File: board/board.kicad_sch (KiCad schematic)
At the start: 22 parts, among them J1 Conn_01x10_Pin, J2 Conn_01x10, J3 Conn_01x20, J5 Conn_01x06, U1 nPM1300-CAXX

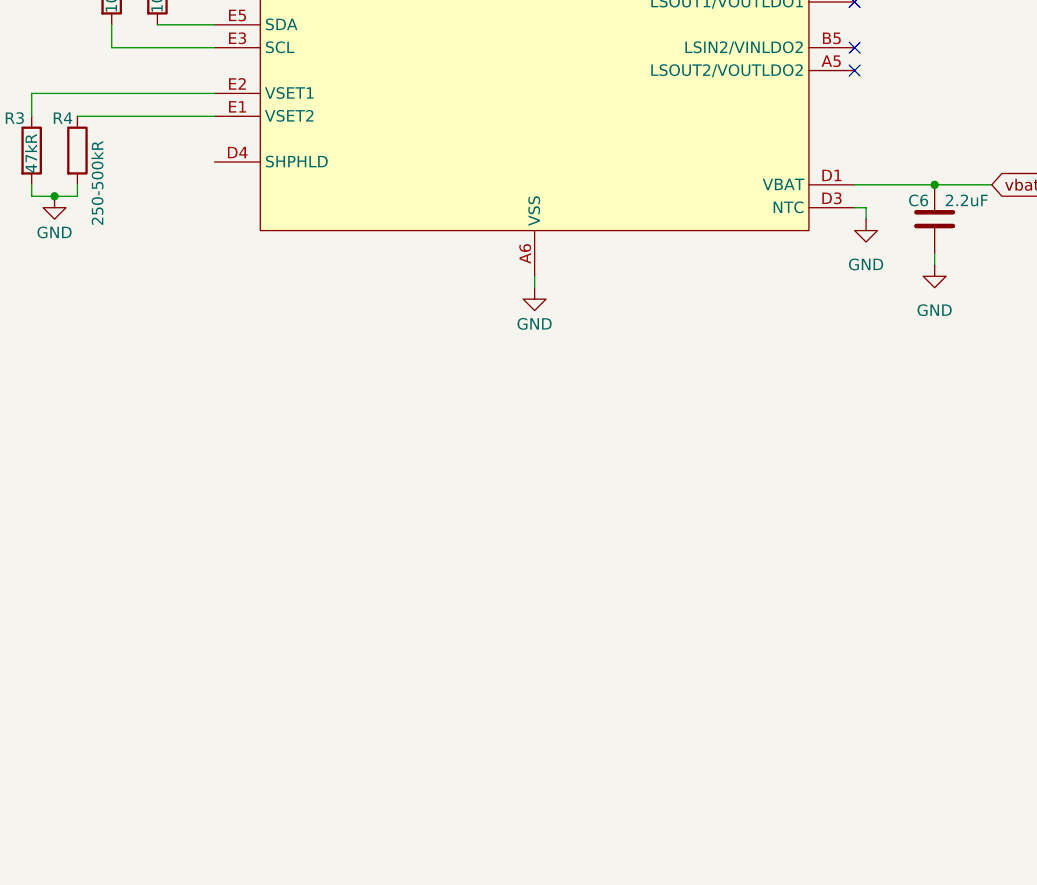
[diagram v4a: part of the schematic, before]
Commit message: board: sch tidy up and battery connector
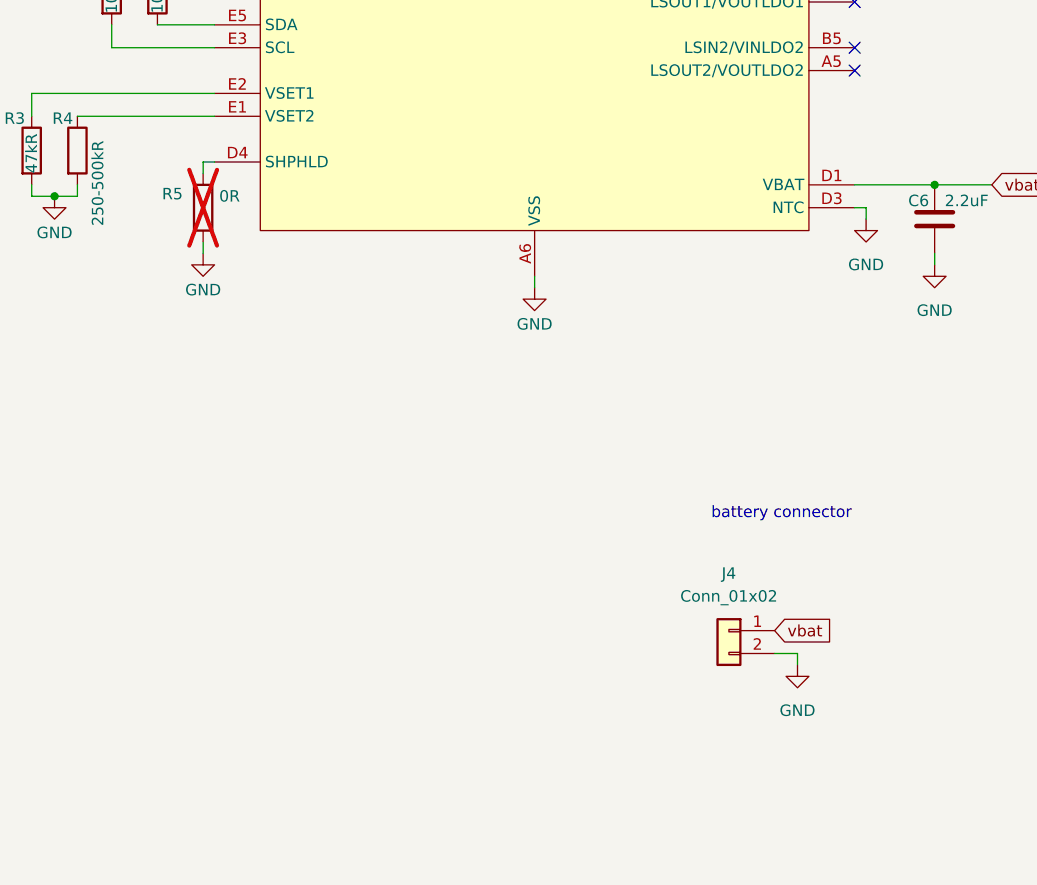
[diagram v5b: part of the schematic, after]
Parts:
- added J4: Conn_01x02, symbol Connector_Generic:Conn_01x02
- added R5: 0R, symbol Device:R
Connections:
- net GND: now also J4.2 (Pin_2), R5.2
- net vbat: now also J4.1 (Pin_1)
- net at U1.D4 (SHPHLD): now also R5.1
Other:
- note added: "battery connector"

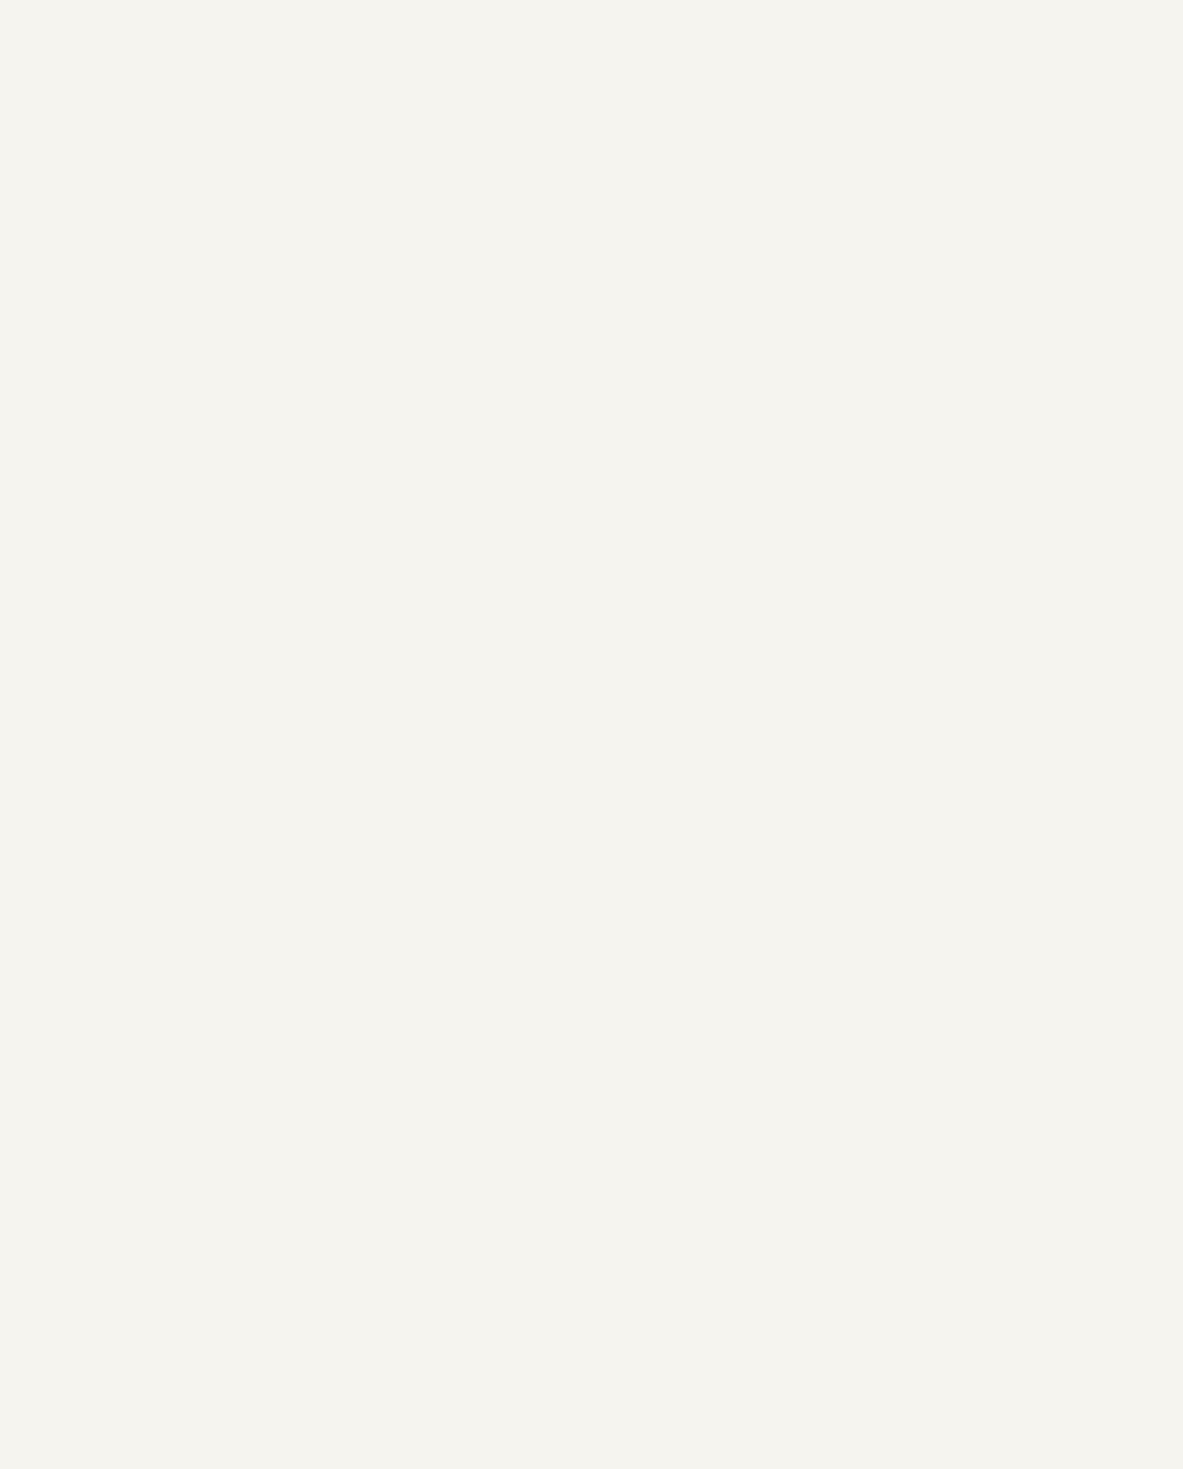
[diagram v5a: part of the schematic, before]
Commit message: board: sch add mcu
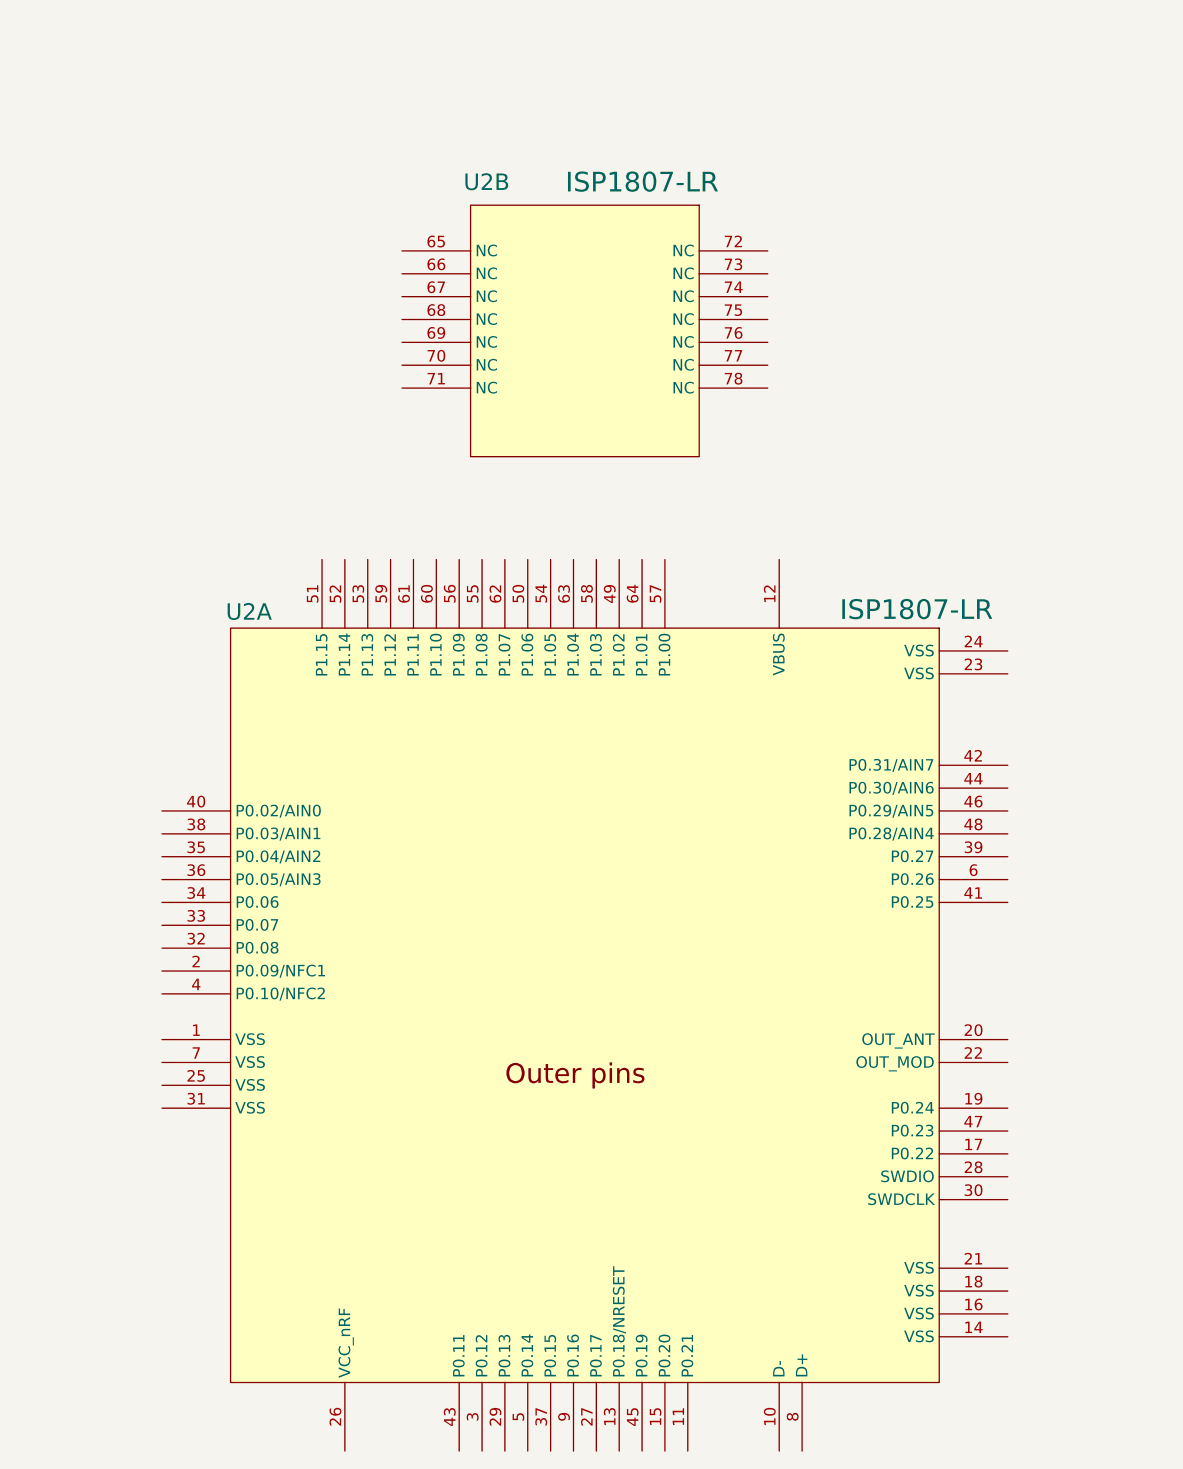
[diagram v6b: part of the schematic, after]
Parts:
- added U2: ${ISP_PART}, ISP1807-LR, symbol nordic-lib-kicad-isp1807:ISP1807-LR

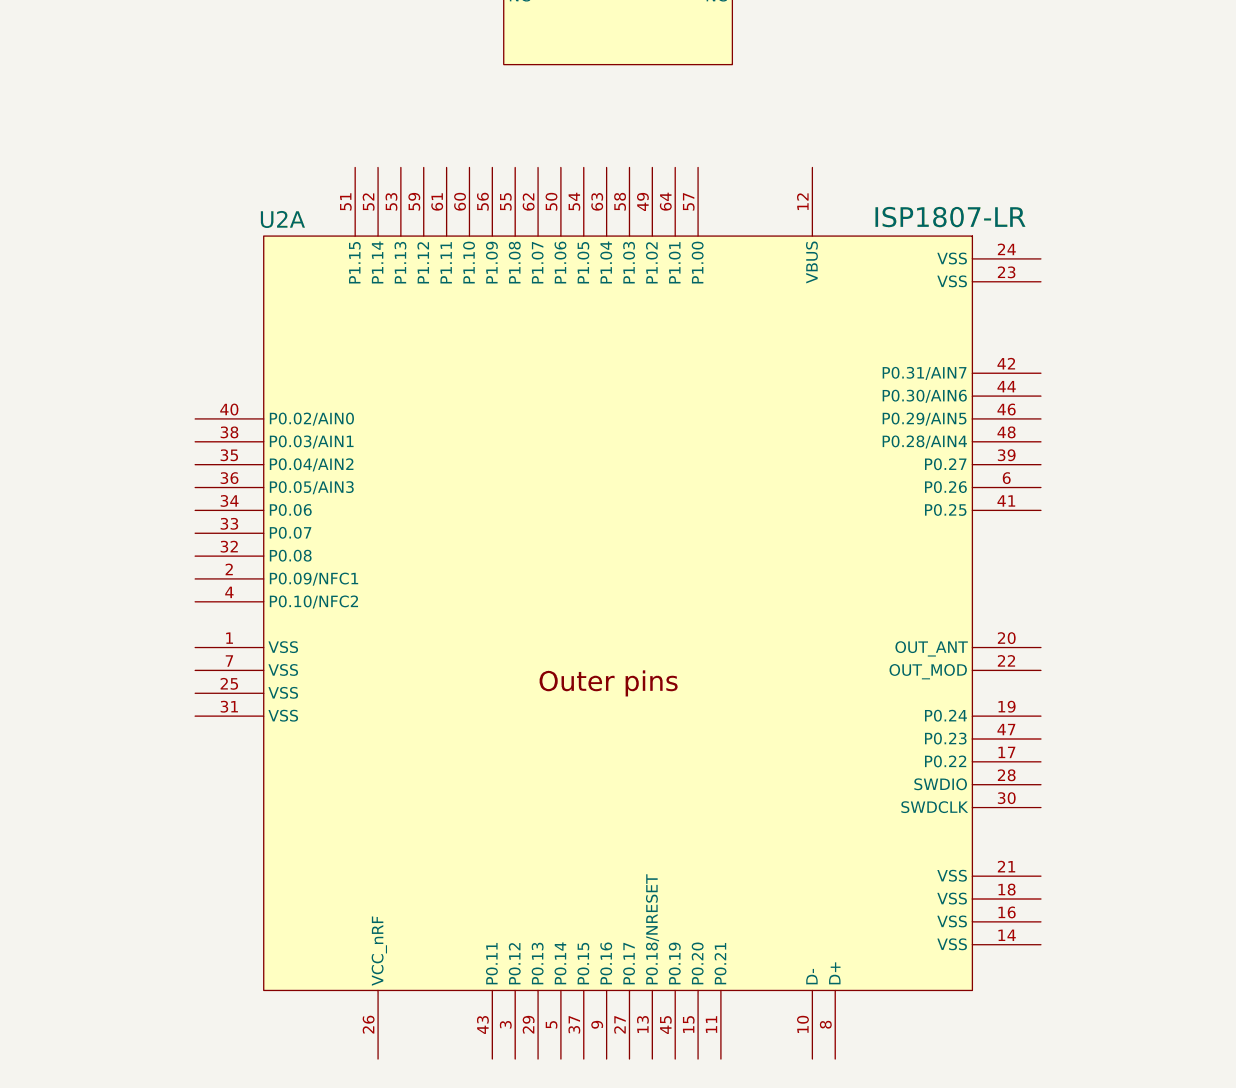
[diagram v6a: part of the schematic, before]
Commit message: board: sch mcu connect power
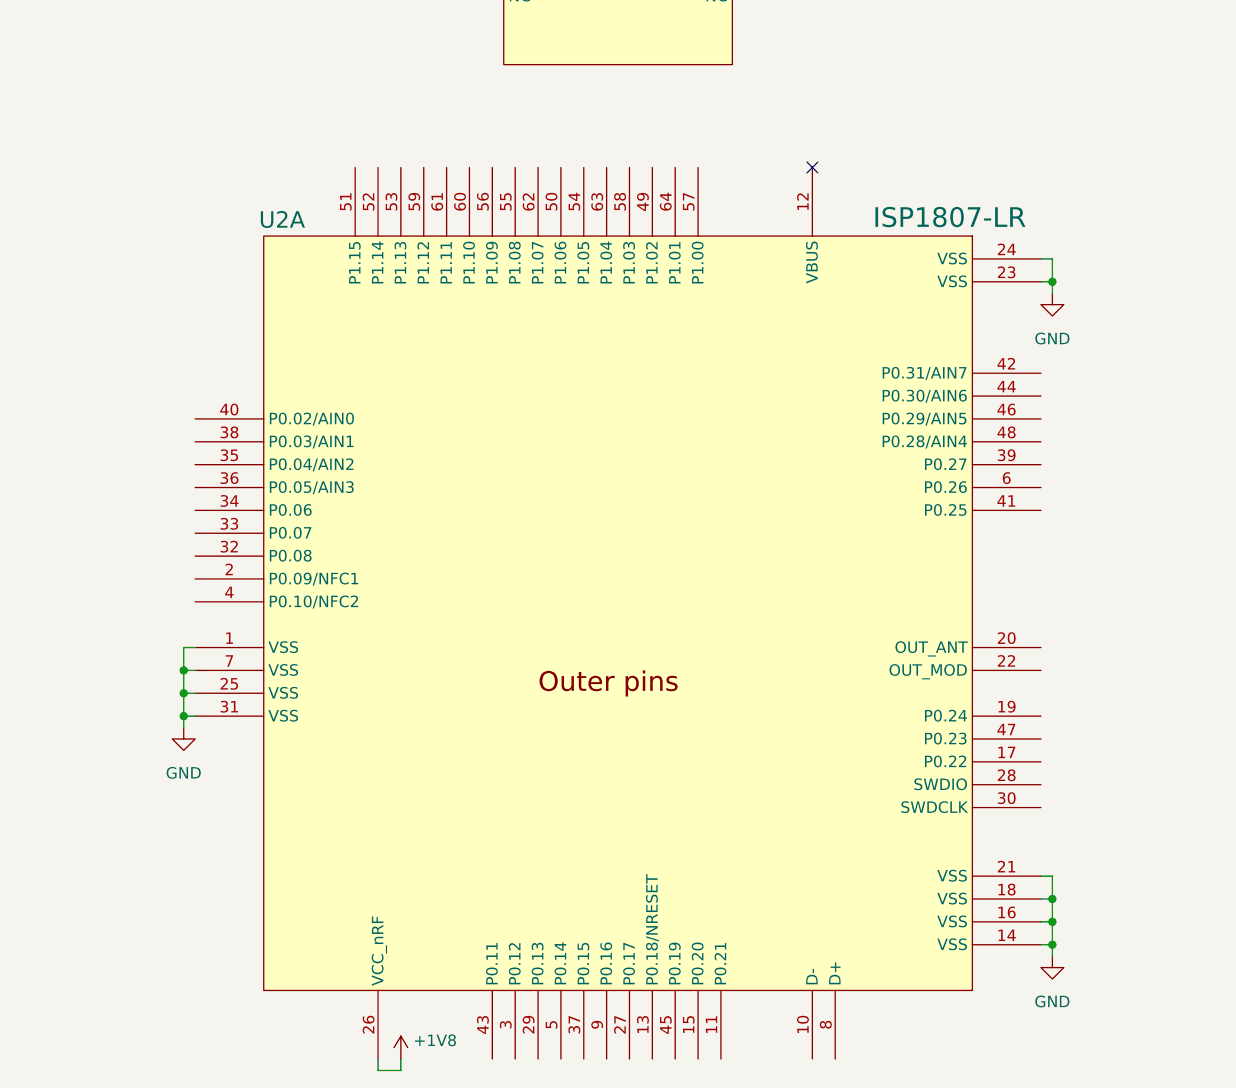
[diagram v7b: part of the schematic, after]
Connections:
- net +1V8: now also U2.26 (VCC_nRF)
- net GND: now also U2.1 (VSS), U2.14 (VSS), U2.16 (VSS), U2.18 (VSS), U2.21 (VSS), U2.23 (VSS), U2.24 (VSS), U2.25 (VSS), U2.31 (VSS), U2.7 (VSS)
- no-connect marks 11 -> 12
